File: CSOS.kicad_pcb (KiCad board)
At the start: 2 copper layers, 49.5 x 67.3 mm, 23 parts, among them P101 CONN_01X02, P102 CONN_01X03, P103 CONN_01X02, P201 CONN_01X01, Q201 BUK9575, U201 LMV358, U401 LM2931D-R

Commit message: Fixing voltage dividers and adding values.
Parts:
- R201: value R -> 68K
- R301: value R -> 28.7K
- RV201, RV301: value POT -> 10K
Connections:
- R201 pad 1: Net-(R201-Pad1) -> 2.7V
- R201 pad 2: GND -> Net-(R201-Pad2)
- R301 pad 1: Net-(R301-Pad1) -> 2.7V
- R301 pad 2: GND -> Net-(R301-Pad2)
- RV201 pad 1: Net-(RV201-Pad1) -> Net-(R201-Pad2)
- RV201 pad 2: 2.7V -> GND
- RV201 pad 3: Net-(R201-Pad1) -> Net-(RV201-Pad3)
- RV301 pad 2: 2.7V -> Net-(R301-Pad2)
- RV301 pad 3: Net-(R301-Pad1) -> GND
- U201 pad 3: Net-(R201-Pad1) -> Net-(R201-Pad2)
- U201 pad 5: Net-(R301-Pad1) -> Net-(R301-Pad2)
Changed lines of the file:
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@@
   (net 7 "/Current Control/Current_Sink+")
   (net 8 "Net-(Q201-Pad3)")
-  (net 9 "Net-(R201-Pad1)")
-  (net 10 "Net-(R202-Pad2)")
-  (net 11 "Net-(R301-Pad1)")
-  (net 12 "Net-(R302-Pad2)")
-  (net 13 "Net-(R401-Pad1)")
-  (net 14 "Net-(R402-Pad2)")
-  (net 15 "Net-(RV201-Pad1)")
-  (net 16 "Net-(RV301-Pad1)")
+  (net 9 "Net-(R202-Pad2)")
+  (net 10 "Net-(R302-Pad2)")
+  (net 11 "Net-(R401-Pad1)")
+  (net 12 "Net-(R402-Pad2)")
+  (net 13 "Net-(RV301-Pad1)")
+  (net 14 "Net-(R201-Pad2)")
+  (net 15 "Net-(R301-Pad2)")
+  (net 16 "Net-(RV201-Pad3)")
   (net_class Default "This is the default net class."
     (clearance 0.2)
@@
     (add_net "Net-(P101-Pad1)")
     (add_net "Net-(Q201-Pad3)")
-    (add_net "Net-(R201-Pad1)")
+    (add_net "Net-(R201-Pad2)")
     (add_net "Net-(R202-Pad2)")
-    (add_net "Net-(R301-Pad1)")
+    (add_net "Net-(R301-Pad2)")
     (add_net "Net-(R302-Pad2)")
     (add_net "Net-(R401-Pad1)")
     (add_net "Net-(R402-Pad2)")
-    (add_net "Net-(RV201-Pad1)")
+    (add_net "Net-(RV201-Pad3)")
     (add_net "Net-(RV301-Pad1)")
   )
@@
       (effects (font (size 1 1) (thickness 0.15)))
     )
-    (fp_text value R (at 0 2.1) (layer F.Fab)
-      (effects (font (size 1 1) (thickness 0.15)))
-    )
-    (fp_line (start -2.4 -1) (end 2.4 -1) (layer F.CrtYd) (width 0.05))
-    (fp_line (start -2.4 1) (end 2.4 1) (layer F.CrtYd) (width 0.05))
-    (fp_line (start -2.4 -1) (end -2.4 1) (layer F.CrtYd) (width 0.05))
-    (fp_line (start 2.4 -1) (end 2.4 1) (layer F.CrtYd) (width 0.05))
-    (fp_line (start 0.6 0.875) (end -0.6 0.875) (layer F.SilkS) (width 0.15))
-    (fp_line (start -0.6 -0.875) (end 0.6 -0.875) (layer F.SilkS) (width 0.15))
-    (pad 1 smd rect (at -1.35 0) (size 1.5 1.3) (layers F.Cu F.Paste F.Mask)
-      (net 9 "Net-(R201-Pad1)"))
-    (pad 2 smd rect (at 1.35 0) (size 1.5 1.3) (layers F.Cu F.Paste F.Mask)
-      (net 2 GND))
+    (fp_text value 68K (at 0 2.1) (layer F.Fab)
+      (effects (font (size 1 1) (thickness 0.15)))
+    )
+    (fp_line (start -2.4 -1) (end 2.4 -1) (layer F.CrtYd) (width 0.05))
+    (fp_line (start -2.4 1) (end 2.4 1) (layer F.CrtYd) (width 0.05))
+    (fp_line (start -2.4 -1) (end -2.4 1) (layer F.CrtYd) (width 0.05))
+    (fp_line (start 2.4 -1) (end 2.4 1) (layer F.CrtYd) (width 0.05))
+    (fp_line (start 0.6 0.875) (end -0.6 0.875) (layer F.SilkS) (width 0.15))
+    (fp_line (start -0.6 -0.875) (end 0.6 -0.875) (layer F.SilkS) (width 0.15))
+    (pad 1 smd rect (at -1.35 0) (size 1.5 1.3) (layers F.Cu F.Paste F.Mask)
+      (net 1 2.7V))
+    (pad 2 smd rect (at 1.35 0) (size 1.5 1.3) (layers F.Cu F.Paste F.Mask)
+      (net 14 "Net-(R201-Pad2)"))
     (model Resistors_SMD.3dshapes/R_0805_HandSoldering.wrl
       (at (xyz 0 0 0))
@@
       (net 5 "/Current Control/FET_Gate"))
     (pad 2 smd rect (at 1.35 0) (size 1.5 1.3) (layers F.Cu F.Paste F.Mask)
-      (net 10 "Net-(R202-Pad2)"))
+      (net 9 "Net-(R202-Pad2)"))
     (model Resistors_SMD.3dshapes/R_0805_HandSoldering.wrl
       (at (xyz 0 0 0))
@@
       (effects (font (size 1 1) (thickness 0.15)))
     )
-    (fp_text value R (at 0 2.1) (layer F.Fab)
-      (effects (font (size 1 1) (thickness 0.15)))
-    )
-    (fp_line (start -2.4 -1) (end 2.4 -1) (layer F.CrtYd) (width 0.05))
-    (fp_line (start -2.4 1) (end 2.4 1) (layer F.CrtYd) (width 0.05))
-    (fp_line (start -2.4 -1) (end -2.4 1) (layer F.CrtYd) (width 0.05))
-    (fp_line (start 2.4 -1) (end 2.4 1) (layer F.CrtYd) (width 0.05))
-    (fp_line (start 0.6 0.875) (end -0.6 0.875) (layer F.SilkS) (width 0.15))
-    (fp_line (start -0.6 -0.875) (end 0.6 -0.875) (layer F.SilkS) (width 0.15))
-    (pad 1 smd rect (at -1.35 0) (size 1.5 1.3) (layers F.Cu F.Paste F.Mask)
-      (net 11 "Net-(R301-Pad1)"))
-    (pad 2 smd rect (at 1.35 0) (size 1.5 1.3) (layers F.Cu F.Paste F.Mask)
-      (net 2 GND))
+    (fp_text value 28.7K (at 0 2.1) (layer F.Fab)
+      (effects (font (size 1 1) (thickness 0.15)))
+    )
+    (fp_line (start -2.4 -1) (end 2.4 -1) (layer F.CrtYd) (width 0.05))
+    (fp_line (start -2.4 1) (end 2.4 1) (layer F.CrtYd) (width 0.05))
+    (fp_line (start -2.4 -1) (end -2.4 1) (layer F.CrtYd) (width 0.05))
+    (fp_line (start 2.4 -1) (end 2.4 1) (layer F.CrtYd) (width 0.05))
+    (fp_line (start 0.6 0.875) (end -0.6 0.875) (layer F.SilkS) (width 0.15))
+    (fp_line (start -0.6 -0.875) (end 0.6 -0.875) (layer F.SilkS) (width 0.15))
+    (pad 1 smd rect (at -1.35 0) (size 1.5 1.3) (layers F.Cu F.Paste F.Mask)
+      (net 1 2.7V))
+    (pad 2 smd rect (at 1.35 0) (size 1.5 1.3) (layers F.Cu F.Paste F.Mask)
+      (net 15 "Net-(R301-Pad2)"))
     (model Resistors_SMD.3dshapes/R_0805_HandSoldering.wrl
       (at (xyz 0 0 0))
@@
       (net 7 "/Current Control/Current_Sink+"))
     (pad 2 smd rect (at 1.35 0) (size 1.5 1.3) (layers F.Cu F.Paste F.Mask)
-      (net 12 "Net-(R302-Pad2)"))
+      (net 10 "Net-(R302-Pad2)"))
     (model Resistors_SMD.3dshapes/R_0805_HandSoldering.wrl
       (at (xyz 0 0 0))
@@
     (fp_line (start -0.6 -0.875) (end 0.6 -0.875) (layer F.SilkS) (width 0.15))
     (pad 1 smd rect (at -1.35 0) (size 1.5 1.3) (layers F.Cu F.Paste F.Mask)
-      (net 12 "Net-(R302-Pad2)"))
+      (net 10 "Net-(R302-Pad2)"))
     (pad 2 smd rect (at 1.35 0) (size 1.5 1.3) (layers F.Cu F.Paste F.Mask)
       (net 2 GND))
@@
     (fp_line (start -0.6 -0.875) (end 0.6 -0.875) (layer F.SilkS) (width 0.15))
     (pad 1 smd rect (at -1.35 0) (size 1.5 1.3) (layers F.Cu F.Paste F.Mask)
-      (net 13 "Net-(R401-Pad1)"))
+      (net 11 "Net-(R401-Pad1)"))
     (pad 2 smd rect (at 1.35 0) (size 1.5 1.3) (layers F.Cu F.Paste F.Mask)
       (net 2 GND))
@@
       (net 1 2.7V))
     (pad 2 smd rect (at 1.35 0) (size 1.5 1.3) (layers F.Cu F.Paste F.Mask)
-      (net 14 "Net-(R402-Pad2)"))
+      (net 12 "Net-(R402-Pad2)"))
     (model Resistors_SMD.3dshapes/R_0805_HandSoldering.wrl
       (at (xyz 0 0 0))
@@
     (fp_line (start -0.6 -0.875) (end 0.6 -0.875) (layer F.SilkS) (width 0.15))
     (pad 1 smd rect (at -1.35 0) (size 1.5 1.3) (layers F.Cu F.Paste F.Mask)
-      (net 14 "Net-(R402-Pad2)"))
+      (net 12 "Net-(R402-Pad2)"))
     (pad 2 smd rect (at 1.35 0) (size 1.5 1.3) (layers F.Cu F.Paste F.Mask)
       (net 2 GND))
@@
       (net 4 "Net-(D301-Pad1)"))
     (pad 6 smd rect (at 0.635 -3.175) (size 0.508 1.143) (layers F.Cu F.Paste F.Mask)
-      (net 12 "Net-(R302-Pad2)"))
+      (net 10 "Net-(R302-Pad2)"))
     (pad 5 smd rect (at 1.905 -3.175) (size 0.508 1.143) (layers F.Cu F.Paste F.Mask)
-      (net 11 "Net-(R301-Pad1)"))
+      (net 15 "Net-(R301-Pad2)"))
     (pad 4 smd rect (at 1.905 3.175) (size 0.508 1.143) (layers F.Cu F.Paste F.Mask)
       (net 2 GND))
     (pad 3 smd rect (at 0.635 3.175) (size 0.508 1.143) (layers F.Cu F.Paste F.Mask)
-      (net 9 "Net-(R201-Pad1)"))
+      (net 14 "Net-(R201-Pad2)"))
     (pad 2 smd rect (at -0.635 3.175) (size 0.508 1.143) (layers F.Cu F.Paste F.Mask)
       (net 8 "Net-(Q201-Pad3)"))
     (pad 1 smd rect (at -1.905 3.175) (size 0.508 1.143) (layers F.Cu F.Paste F.Mask)
-      (net 10 "Net-(R202-Pad2)"))
+      (net 9 "Net-(R202-Pad2)"))
     (model SMD_Packages.3dshapes/SOIC-8-N.wrl
       (at (xyz 0 0 0))
@@
       (net 2 GND))
     (pad 5 smd rect (at 1.905 -3.175) (size 0.508 1.143) (layers F.Cu F.Paste F.Mask)
-      (net 13 "Net-(R401-Pad1)"))
+      (net 11 "Net-(R401-Pad1)"))
     (pad 4 smd rect (at 1.905 3.175) (size 0.508 1.143) (layers F.Cu F.Paste F.Mask)
-      (net 14 "Net-(R402-Pad2)"))
+      (net 12 "Net-(R402-Pad2)"))
     (pad 3 smd rect (at 0.635 3.175) (size 0.508 1.143) (layers F.Cu F.Paste F.Mask)
       (net 2 GND))
@@
       (effects (font (size 1 1) (thickness 0.15)))
     )
-    (fp_text value POT (at 0 -6.7 90) (layer F.Fab)
+    (fp_text value 10K (at 0 -6.7 90) (layer F.Fab)
       (effects (font (size 1 1) (thickness 0.15)))
     )
@@
     (pad "" np_thru_hole oval (at -5.1 -3.3 90) (size 2 2.2) (drill oval 2 2.2) (layers *.Cu *.Mask F.SilkS))
     (pad 1 thru_hole circle (at -2.5 0 90) (size 2 2) (drill 1) (layers *.Cu *.Mask F.SilkS)
-      (net 15 "Net-(RV201-Pad1)"))
+      (net 14 "Net-(R201-Pad2)"))
     (pad 2 thru_hole circle (at 0 0 90) (size 2 2) (drill 1) (layers *.Cu *.Mask F.SilkS)
-      (net 1 2.7V))
+      (net 2 GND))
     (pad 3 thru_hole circle (at 2.5 0 90) (size 2 2) (drill 1) (layers *.Cu *.Mask F.SilkS)
-      (net 9 "Net-(R201-Pad1)"))
+      (net 16 "Net-(RV201-Pad3)"))
     (pad "" np_thru_hole oval (at 5.1 -3.3 90) (size 2 2.2) (drill oval 2 2.2) (layers *.Cu *.Mask F.SilkS))
   )
@@
       (effects (font (size 1 1) (thickness 0.15)))
     )
-    (fp_text value POT (at 0 -6.7 270) (layer F.Fab)
+    (fp_text value 10K (at 0 -6.7 270) (layer F.Fab)
       (effects (font (size 1 1) (thickness 0.15)))
     )
@@
     (pad "" np_thru_hole oval (at -5.1 -3.3 270) (size 2 2.2) (drill oval 2 2.2) (layers *.Cu *.Mask F.SilkS))
     (pad 1 thru_hole circle (at -2.5 0 270) (size 2 2) (drill 1) (layers *.Cu *.Mask F.SilkS)
-      (net 16 "Net-(RV301-Pad1)"))
+      (net 13 "Net-(RV301-Pad1)"))
     (pad 2 thru_hole circle (at 0 0 270) (size 2 2) (drill 1) (layers *.Cu *.Mask F.SilkS)
-      (net 1 2.7V))
+      (net 15 "Net-(R301-Pad2)"))
     (pad 3 thru_hole circle (at 2.5 0 270) (size 2 2) (drill 1) (layers *.Cu *.Mask F.SilkS)
-      (net 11 "Net-(R301-Pad1)"))
+      (net 2 GND))
     (pad "" np_thru_hole oval (at 5.1 -3.3 270) (size 2 2.2) (drill oval 2 2.2) (layers *.Cu *.Mask F.SilkS))
   )

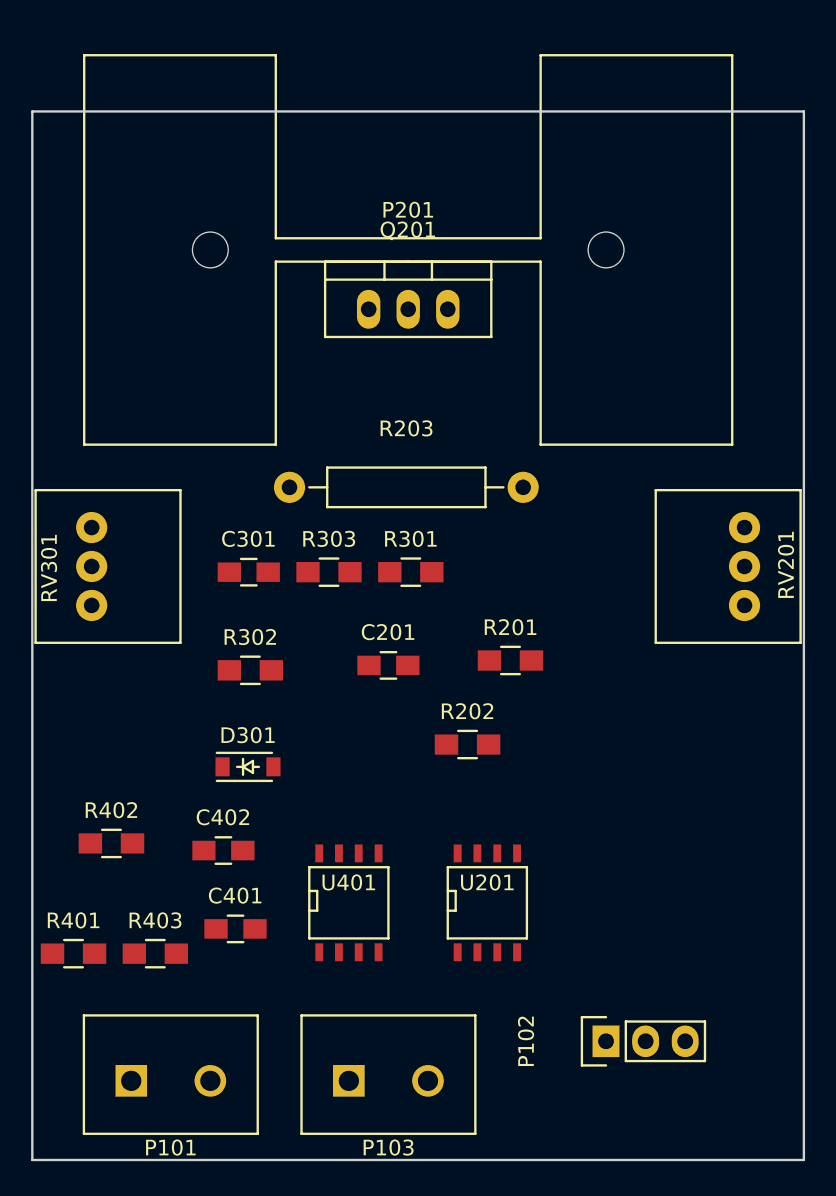
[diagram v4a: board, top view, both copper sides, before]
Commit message: Starting parts placement.
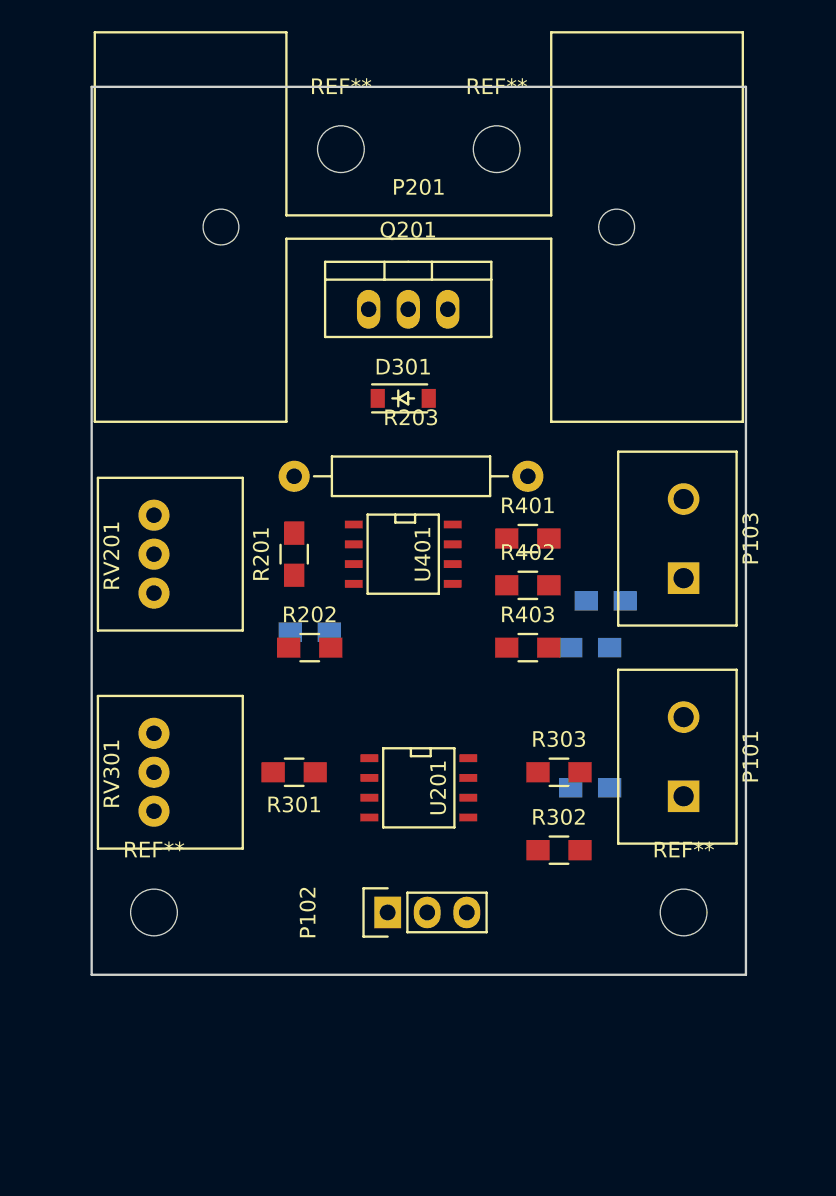
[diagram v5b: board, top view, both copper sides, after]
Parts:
- added REF**: MountingHole_3mm, Mounting_Holes:MountingHole_3mm, F.Cu at (153.0, 71.0)
- added REF**: MountingHole_3mm, Mounting_Holes:MountingHole_3mm, F.Cu at (131.0, 120.0)
- added REF**: MountingHole_3mm, Mounting_Holes:MountingHole_3mm, F.Cu at (165.0, 120.0)
- added REF**: MountingHole_3mm, Mounting_Holes:MountingHole_3mm, F.Cu at (143.0, 71.0)
- C201, C301, C401, C402: moved to B.Cu
- moved P103 39.6 mm to (165.0, 96.0), turned to 90 degrees
- moved R401 39.5 mm to (155.0, 96.0)
- moved P101 38.9 mm to (165.0, 110.0), turned to 90 degrees
- moved RV201 37.9 mm to (131.0, 97.0), turned to 270 degrees
- moved R402 31.4 mm to (155.0, 99.0)
- moved R403 30.9 mm to (155.0, 103.0)
- moved C402 29.3 mm to (160.0, 100.0)
- moved C401 29.1 mm to (159.0, 103.0)
- moved C301 25.9 mm to (159.0, 112.0)
- moved D301 25.7 mm to (147.0, 87.0)
- moved R302 22.9 mm to (157.0, 116.0)
- moved U401 22.7 mm to (147.0, 97.0), turned to 270 degrees
- moved R303 19.6 mm to (157.0, 111.0)
- moved P102 16.3 mm to (146.0, 120.0)
- moved R201 15.5 mm to (140.0, 97.0), turned to 90 degrees
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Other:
- board size 49.5 x 67.3 mm -> 42 x 57 mm

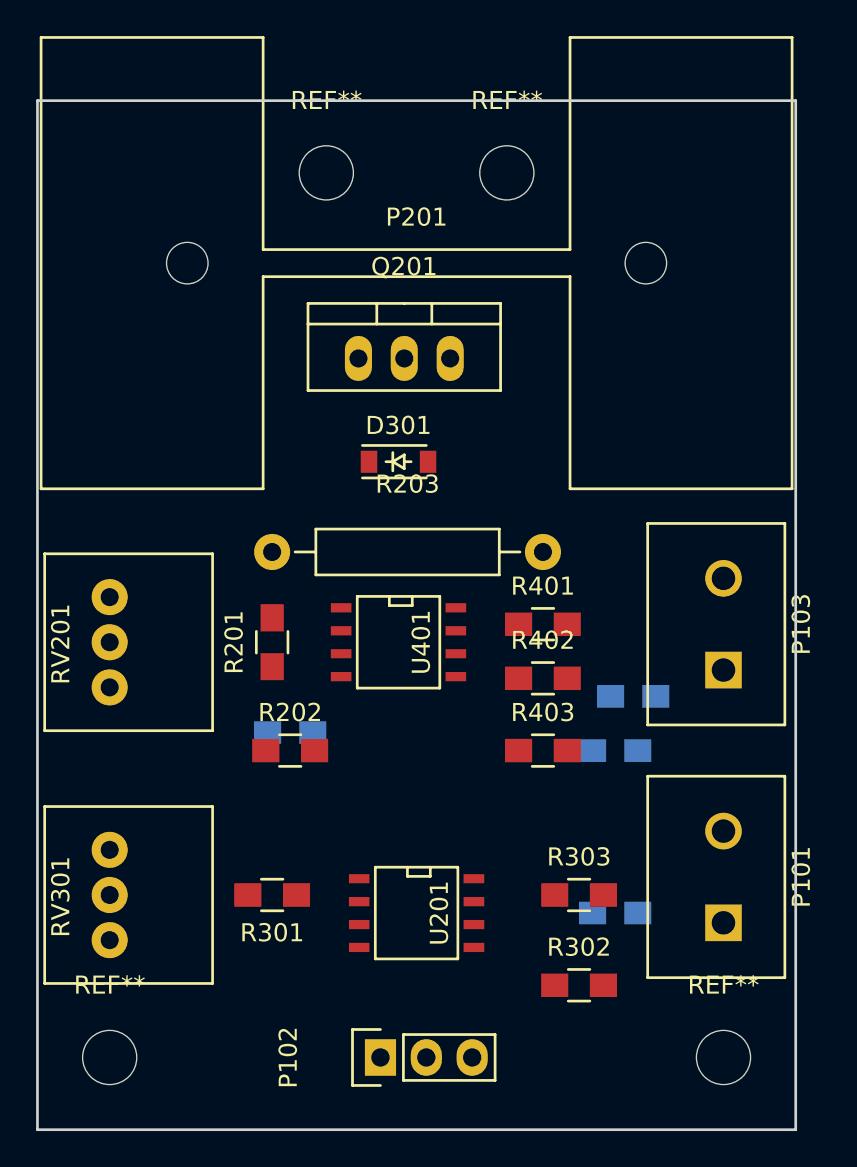
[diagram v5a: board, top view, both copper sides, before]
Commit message: Fixing FET.
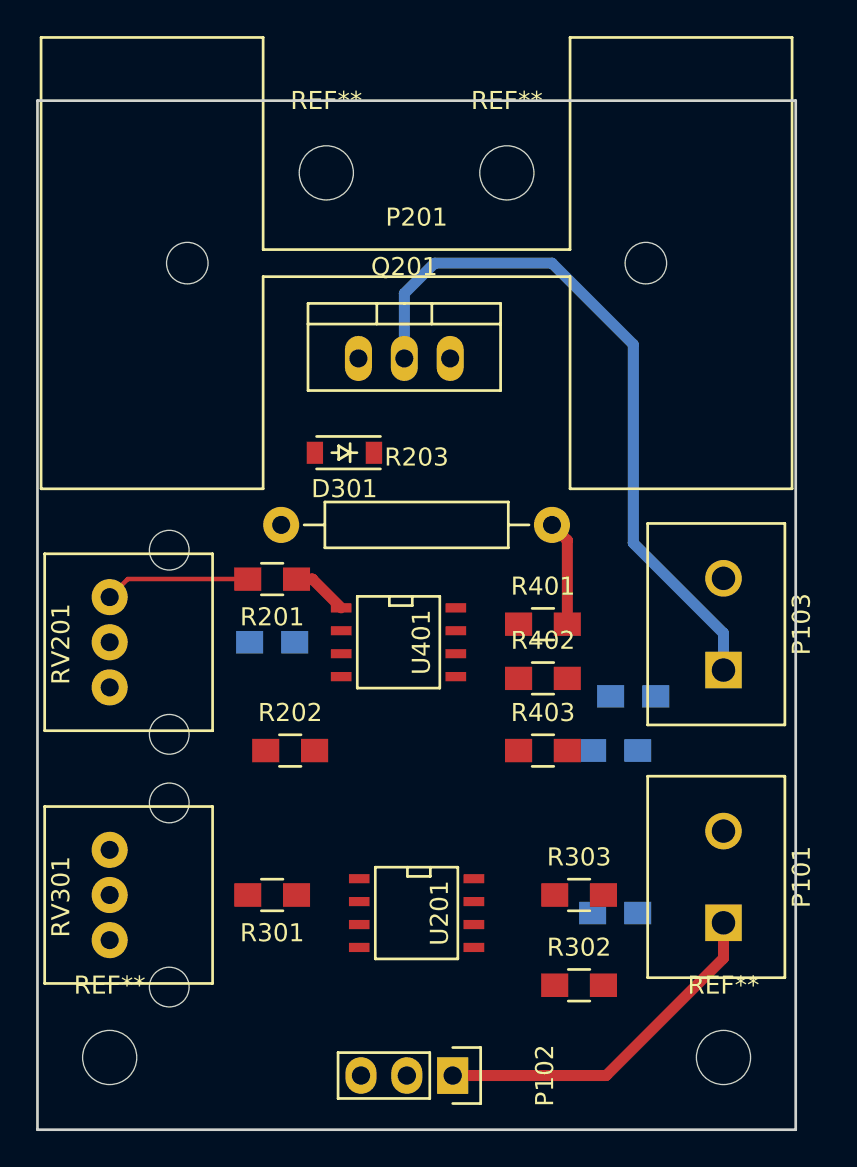
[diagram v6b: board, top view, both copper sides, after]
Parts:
- Q201: value BUK9575 -> Q_NMOS_GDS
- moved C201 5.10 mm to (140.0, 97.0)
- moved P102 4.12 mm to (150.0, 121.0), turned to 270 degrees
- moved R201 3.50 mm to (140.0, 93.5), turned to 180 degrees
- moved D301 3.04 mm to (144.0, 86.5), turned to 180 degrees
- moved R203 1.58 mm to (140.5, 90.5)
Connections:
- Q201 pad 1: /Current Control/Current_Sink+ -> /Current Control/FET_Gate
- Q201 pad 2: /Current Control/FET_Gate -> /Current Control/Current_Sink+
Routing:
- net /Current Control/Current_Sink+: track 0.00 -> 39.0 mm
- net Net-(P101-Pad1): track 0.00 -> 19.7 mm
- net Net-(R201-Pad2): track 0.00 -> 8.06 mm
- net GND: track 0.00 -> 5.85 mm
- net 2.7V: track 0.00 -> 3.14 mm
- added copper zone on B.Cu, net GND
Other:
- net class Power added: clearance 0.3048, trace_width 0.6096, via_dia 1.143, via_drill 0.762

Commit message: Layout connected.
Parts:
- removed C301: C, Capacitors_SMD:C_0805_HandSoldering
- moved R303 31.9 mm to (131.0, 92.5), turned to 90 degrees
- moved R302 26.6 mm to (135.0, 101.0), turned to 180 degrees
- moved RV201 25.5 mm to (149.0, 115.0), turned to 0 degrees
- moved R301 19.1 mm to (138.0, 92.0)
- moved U201 18.4 mm to (138.0, 96.5)
- moved P102 17.4 mm to (158.0, 105.5), turned to 180 degrees
- moved R401 16.9 mm to (141.0, 105.5), turned to 90 degrees
- moved R202 15.4 mm to (144.5, 88.0), turned to 270 degrees
- moved R203 13.0 mm to (151.5, 83.5), turned to 300 degrees
- moved C402 8.90 mm to (153.0, 94.5)
- moved R201 8.49 mm to (146.0, 99.5), turned to 90 degrees
- moved U401 8.06 mm to (148.0, 105.0)
- moved RV301 5.32 mm to (134.5, 115.0), turned to 0 degrees
- moved C401 4.27 mm to (163.0, 101.5)
- moved R403 3.54 mm to (152.5, 100.5)
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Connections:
- U201 pad 1: Net-(R202-Pad2) -> Net-(D301-Pad1)
- U201 pad 2: Net-(Q201-Pad3) -> Net-(R302-Pad2)
- U201 pad 3: Net-(R201-Pad2) -> Net-(R301-Pad2)
- U201 pad 5: Net-(R301-Pad2) -> Net-(R201-Pad2)
- U201 pad 6: Net-(R302-Pad2) -> Net-(Q201-Pad3)
- U201 pad 7: Net-(D301-Pad1) -> Net-(R202-Pad2)
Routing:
- net /Current Control/Current_Sink+: track 39.0 -> 77.7 mm, vias 0 -> 1
- net 2.7V: track 3.14 -> 33.1 mm, vias 0 -> 2
- net Net-(R301-Pad2): track 0.00 -> 28.0 mm, vias 0 -> 1
- net GND: track 5.85 -> 31.9 mm, vias 0 -> 3
- net Net-(R201-Pad2): track 8.06 -> 30.2 mm, vias 0 -> 2
- net Net-(Q201-Pad3): track 0.00 -> 22.1 mm
- net Net-(R402-Pad2): track 0.00 -> 15.1 mm, vias 0 -> 2
- net /Current Control/FET_Gate: track 0.27 -> 14.0 mm
- net Net-(R302-Pad2): track 0.00 -> 13.0 mm
- net Net-(R401-Pad1): track 0.00 -> 11.6 mm
- net Net-(D301-Pad1): track 0.00 -> 11.5 mm
- net /Power Regulation/Vin: track 0.00 -> 11.2 mm
- net Net-(P101-Pad1): track 19.7 -> 9.98 mm
- net Net-(R202-Pad2): track 0.00 -> 8.14 mm

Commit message: Gerber generation.
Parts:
- moved REF** 20.1 mm to (172.5, 76.0)
- moved REF** 20.1 mm to (123.5, 76.0)
- moved REF** 8.75 mm to (172.5, 115.5)
- moved REF** 8.60 mm to (123.5, 115.5)
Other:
- board size 42 x 57 mm -> 56 x 46 mm
- board text added: "+ -"
- board text added: "Battery"
- board text added: "Current"
- board text added: "Current Sink Rev: -"
- board text added: "Joseph Allan"
- board text added: "V"
- board text added: "i"
